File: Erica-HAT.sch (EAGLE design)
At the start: 64 parts, among them IC1 MEGA8-AI, K1 PIN20X2, Q1 12M, Q2 2.5A/30V, U1 EEPROM24, U2 TMP102, U3 AD5241BRZ1M, U4 MMDT2907A-7-F, U5 +12v

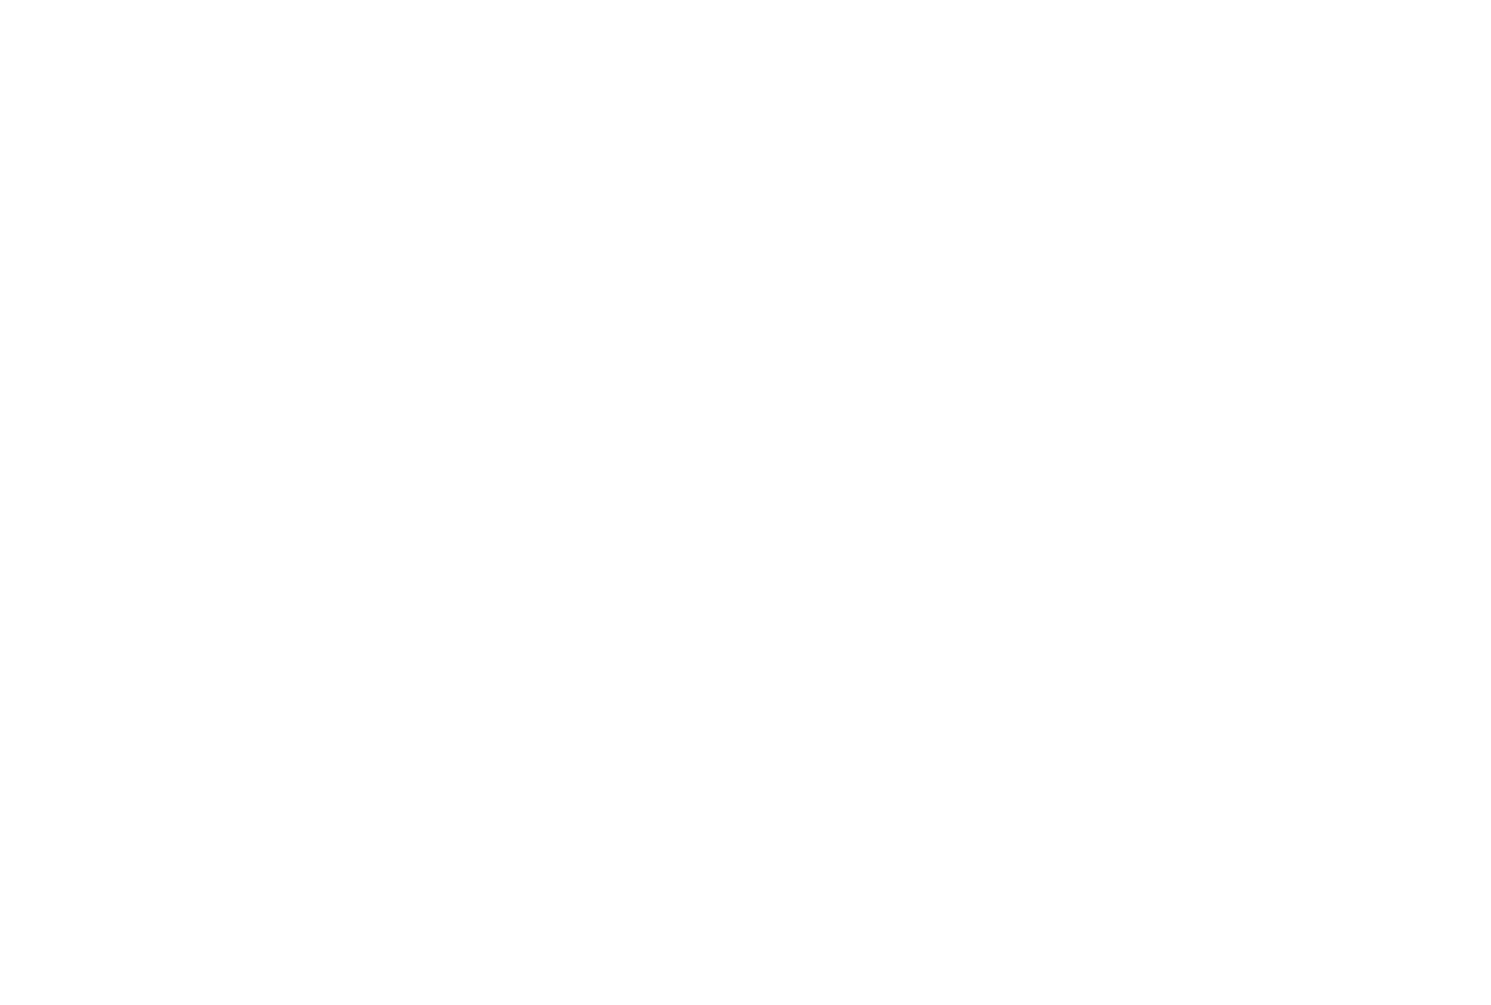
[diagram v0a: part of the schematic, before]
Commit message: Added USB to serial for debug
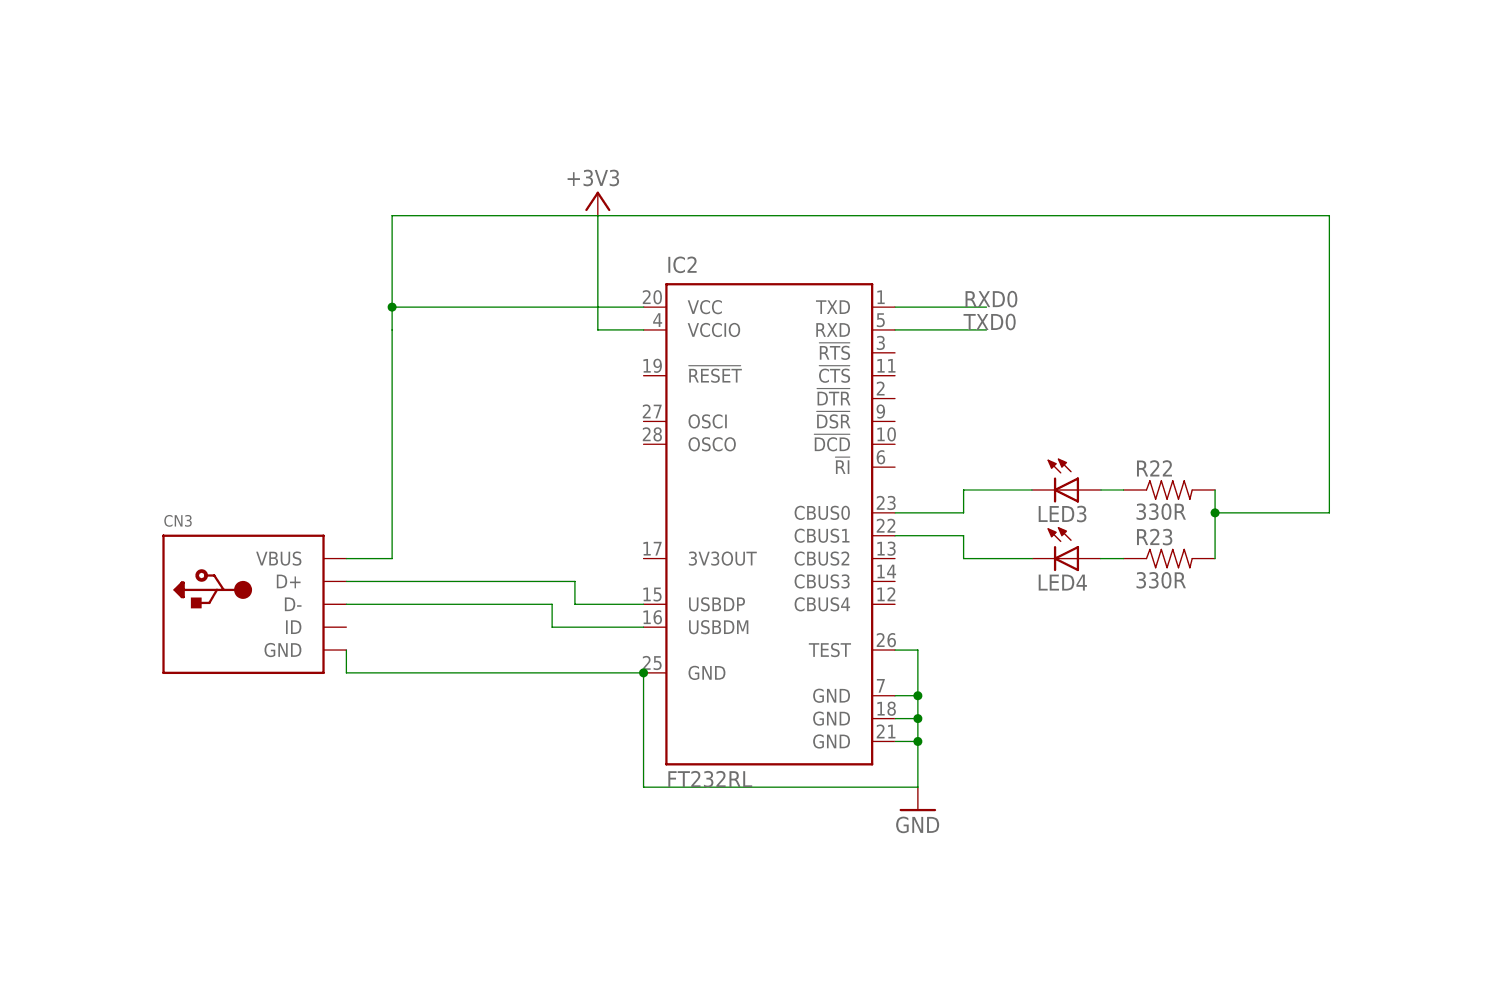
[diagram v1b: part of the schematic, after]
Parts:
- added CN3: (no value), adafruit:USBMINIB
- added IC2: FT232RL, ftdichip:FT232RL
- added LED3, LED4: (no value), adafruit:LEDCHIP-LED0603
- added R22, R23: 330R, SparkFun-Passives:RESISTOR0603-RES
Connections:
- new net N$44: LED3.A, R22.1
- new net N$45: CN3.D-, IC2.USBDM
- new net N$47: CN3.D+, IC2.USBDP
- new net N$48: LED4.A, R23.1
- new net N$49: IC2.CBUS0, LED3.C
- new net N$50: IC2.CBUS1, LED4.C
- new net N$51: CN3.VBUS, IC2.VCC, R22.2, R23.2
- net +3V3: now also IC2.VCCIO
- net GND: now also CN3.GND, IC2.GND, IC2.GND@1, IC2.GND@2, IC2.GND@A, IC2.TEST
- net RXD0: now also IC2.TXD
- net TXD0: now also IC2.RXD

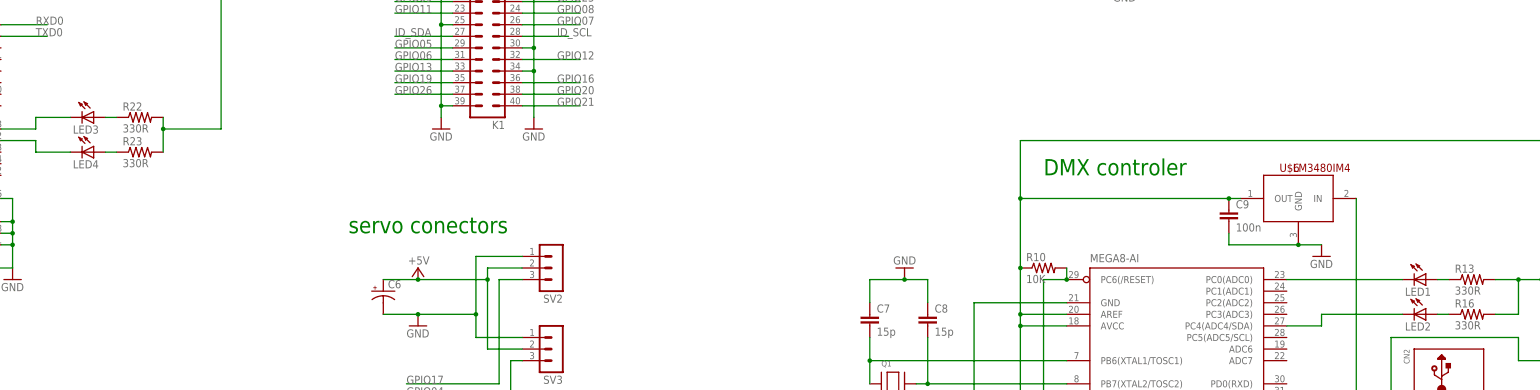
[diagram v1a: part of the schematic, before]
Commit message: Added silkscreen labels
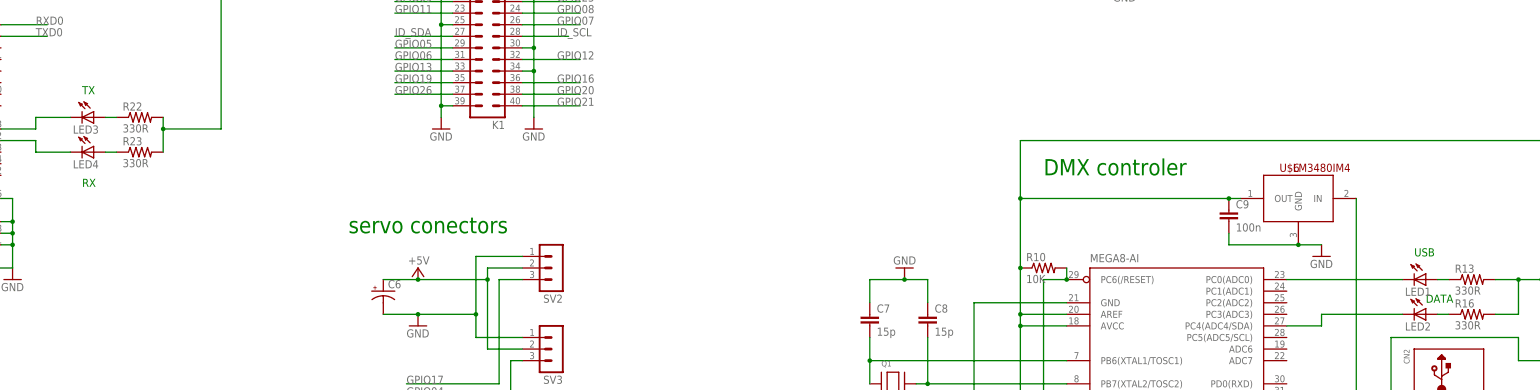
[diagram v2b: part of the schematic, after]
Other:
- note added: "DATA"
- note added: "RX"
- note added: "TX"
- note added: "USB"
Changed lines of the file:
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@@
 <grid distance="0.1" unitdist="inch" unit="inch" style="lines" multiple="1" display="no" altdistance="0.01" altunitdist="inch" altunit="inch"/>
 <layers>
-<layer number="1" name="Top" color="4" fill="1" visible="no" active="no"/>
-<layer number="2" name="Route2" color="1" fill="3" visible="no" active="no"/>
-<layer number="3" name="Route3" color="4" fill="3" visible="no" active="no"/>
-<layer number="14" name="Route14" color="1" fill="6" visible="no" active="no"/>
-<layer number="15" name="Route15" color="4" fill="6" visible="no" active="no"/>
-<layer number="16" name="Bottom" color="1" fill="1" visible="no" active="no"/>
-<layer number="17" name="Pads" color="2" fill="1" visible="no" active="no"/>
-<layer number="18" name="Vias" color="2" fill="1" visible="no" active="no"/>
-<layer number="19" name="Unrouted" color="6" fill="1" visible="no" active="no"/>
-<layer number="20" name="Dimension" color="15" fill="1" visible="no" active="no"/>
-<layer number="21" name="tPlace" color="7" fill="1" visible="no" active="no"/>
-<layer number="22" name="bPlace" color="7" fill="1" visible="no" active="no"/>
-<layer number="23" name="tOrigins" color="15" fill="1" visible="no" active="no"/>
-<layer number="24" name="bOrigins" color="15" fill="1" visible="no" active="no"/>
-<layer number="25" name="tNames" color="7" fill="1" visible="no" active="no"/>
-<layer number="26" name="bNames" color="7" fill="1" visible="no" active="no"/>
-<layer number="27" name="tValues" color="7" fill="1" visible="no" active="no"/>
-<layer number="28" name="bValues" color="7" fill="1" visible="no" active="no"/>
+<layer number="1" name="Top" color="4" fill="1" visible="yes" active="no"/>
+<layer number="2" name="Route2" color="1" fill="3" visible="yes" active="no"/>
+<layer number="3" name="Route3" color="4" fill="3" visible="yes" active="no"/>
+<layer number="14" name="Route14" color="1" fill="6" visible="yes" active="no"/>
+<layer number="15" name="Route15" color="4" fill="6" visible="yes" active="no"/>
+<layer number="16" name="Bottom" color="1" fill="1" visible="yes" active="no"/>
+<layer number="17" name="Pads" color="2" fill="1" visible="yes" active="no"/>
+<layer number="18" name="Vias" color="2" fill="1" visible="yes" active="no"/>
+<layer number="19" name="Unrouted" color="6" fill="1" visible="yes" active="no"/>
+<layer number="20" name="Dimension" color="15" fill="1" visible="yes" active="no"/>
+<layer number="21" name="tPlace" color="7" fill="1" visible="yes" active="no"/>
+<layer number="22" name="bPlace" color="7" fill="1" visible="yes" active="no"/>
+<layer number="23" name="tOrigins" color="15" fill="1" visible="yes" active="no"/>
+<layer number="24" name="bOrigins" color="15" fill="1" visible="yes" active="no"/>
+<layer number="25" name="tNames" color="7" fill="1" visible="yes" active="no"/>
+<layer number="26" name="bNames" color="7" fill="1" visible="yes" active="no"/>
+<layer number="27" name="tValues" color="7" fill="1" visible="yes" active="no"/>
+<layer number="28" name="bValues" color="7" fill="1" visible="yes" active="no"/>
 <layer number="29" name="tStop" color="7" fill="3" visible="no" active="no"/>
 <layer number="30" name="bStop" color="7" fill="6" visible="no" active="no"/>
@@
 <layer number="35" name="tGlue" color="7" fill="4" visible="no" active="no"/>
 <layer number="36" name="bGlue" color="7" fill="5" visible="no" active="no"/>
-<layer number="37" name="tTest" color="7" fill="1" visible="no" active="no"/>
-<layer number="38" name="bTest" color="7" fill="1" visible="no" active="no"/>
+<layer number="37" name="tTest" color="7" fill="1" visible="yes" active="no"/>
+<layer number="38" name="bTest" color="7" fill="1" visible="yes" active="no"/>
 <layer number="39" name="tKeepout" color="4" fill="11" visible="no" active="no"/>
 <layer number="40" name="bKeepout" color="1" fill="11" visible="no" active="no"/>
@@
 <layer number="44" name="Drills" color="7" fill="1" visible="no" active="no"/>
 <layer number="45" name="Holes" color="7" fill="1" visible="no" active="no"/>
-<layer number="46" name="Milling" color="3" fill="1" visible="no" active="no"/>
-<layer number="47" name="Measures" color="7" fill="1" visible="no" active="no"/>
-<layer number="48" name="Document" color="7" fill="1" visible="no" active="no"/>
-<layer number="49" name="Reference" color="7" fill="1" visible="no" active="no"/>
-<layer number="50" name="dxf" color="7" fill="1" visible="no" active="no"/>
-<layer number="51" name="tDocu" color="7" fill="1" visible="no" active="no"/>
-<layer number="52" name="bDocu" color="7" fill="1" visible="no" active="no"/>
-<layer number="53" name="tGND_GNDA" color="7" fill="1" visible="no" active="no"/>
-<layer number="54" name="bGND_GNDA" color="7" fill="1" visible="no" active="no"/>
-<layer number="56" name="wert" color="7" fill="1" visible="no" active="no"/>
-<layer number="57" name="tCAD" color="7" fill="1" visible="no" active="no"/>
-<layer number="59" name="tCarbon" color="7" fill="1" visible="no" active="no"/>
-<layer number="60" name="bCarbon" color="7" fill="1" visible="no" active="no"/>
+<layer number="46" name="Milling" color="3" fill="1" visible="yes" active="no"/>
+<layer number="47" name="Measures" color="7" fill="1" visible="yes" active="no"/>
+<layer number="48" name="Document" color="7" fill="1" visible="yes" active="no"/>
+<layer number="49" name="Reference" color="7" fill="1" visible="yes" active="no"/>
+<layer number="50" name="dxf" color="7" fill="1" visible="yes" active="no"/>
+<layer number="51" name="tDocu" color="7" fill="1" visible="yes" active="no"/>
+<layer number="52" name="bDocu" color="7" fill="1" visible="yes" active="no"/>
+<layer number="53" name="tGND_GNDA" color="7" fill="1" visible="yes" active="no"/>
+<layer number="54" name="bGND_GNDA" color="7" fill="1" visible="yes" active="no"/>
+<layer number="56" name="wert" color="7" fill="1" visible="yes" active="no"/>
+<layer number="57" name="tCAD" color="7" fill="1" visible="yes" active="no"/>
+<layer number="59" name="tCarbon" color="7" fill="1" visible="yes" active="no"/>
+<layer number="60" name="bCarbon" color="7" fill="1" visible="yes" active="no"/>
 <layer number="90" name="Modules" color="7" fill="1" visible="yes" active="yes"/>
 <layer number="91" name="Nets" color="2" fill="1" visible="yes" active="yes"/>
@@
 <text x="205.74" y="152.4" size="3.556" layer="91">GPIO pinout</text>
 <text x="-129.54" y="322.58" size="3.556" layer="91">Reverse Power Protection</text>
+<text x="-30.48" y="96.52" size="1.778" layer="91">TX</text>
+<text x="-30.48" y="76.2" size="1.778" layer="91">RX</text>
+<text x="261.62" y="60.96" size="1.778" layer="91">USB</text>
+<text x="264.16" y="50.8" size="1.778" layer="91">DATA</text>
 </plain>
 <instances>
